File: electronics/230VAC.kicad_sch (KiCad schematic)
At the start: 11 parts, among them J21 Conn_01x02, J22 Conn_01x02, U13 CNY17-1, U17 H11AA1

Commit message: no tracks, but placement looks good
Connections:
- net GND is gone; now on net GND_LP: C9.2, U17.4
- net P_230VAC: now reaches J21.1 (Pin_1), R23.1
- net N_230VAC: now reaches J21.2 (Pin_2), R24.1
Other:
- moved on the sheet: J21
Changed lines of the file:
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@@
-	(wire
-		(pts
-			(xy 81.28 67.31) (xy 76.2 67.31)
-		)
-		(stroke
-			(width 0)
-			(type default)
-		)
-	)
 	(wire
 		(pts
@@
 	(wire
 		(pts
-			(xy 81.28 66.04) (xy 81.28 67.31)
+			(xy 81.28 68.58) (xy 81.28 66.04)
 		)
 		(stroke
@@
 	(wire
 		(pts
-			(xy 76.2 69.85) (xy 81.28 69.85)
-		)
-		(stroke
-			(width 0)
-			(type default)
-		)
-	)
-	(wire
-		(pts
-			(xy 81.28 69.85) (xy 81.28 71.12)
+			(xy 58.42 71.12) (xy 83.82 71.12)
 		)
 		(stroke
@@
 	(wire
 		(pts
-			(xy 81.28 71.12) (xy 83.82 71.12)
-		)
-		(stroke
-			(width 0)
-			(type default)
-		)
-	)
-	(wire
-		(pts
 			(xy 57.15 107.95) (xy 64.77 107.95)
 		)
@@
 	(wire
 		(pts
+			(xy 58.42 68.58) (xy 81.28 68.58)
+		)
+		(stroke
+			(width 0)
+			(type default)
+		)
+	)
+	(wire
+		(pts
 			(xy 120.65 120.65) (xy 147.32 120.65)
 		)
@@
 	)
 	(rectangle
-		(start 64.77 48.26)
+		(start 52.07 48.26)
 		(end 149.86 85.09)
 		(stroke
@@
 		)
 	)
-	(label "V_Bat"
-		(at 110.49 96.52 0)
+	(label "N_230VAC"
+		(at 67.31 71.12 0)
 		(fields_autoplaced yes)
 		(effects
@@
 		)
 	)
+	(label "P_230VAC"
+		(at 67.31 68.58 0)
+		(fields_autoplaced yes)
+		(effects
+			(font
+				(size 1.27 1.27)
+			)
+			(justify left bottom)
+		)
+	)
+	(label "V_Bat"
+		(at 110.49 96.52 0)
+		(fields_autoplaced yes)
+		(effects
+			(font
+				(size 1.27 1.27)
+			)
+			(justify left bottom)
+		)
+	)
 	(hierarchical_label "AC_DETECT"
 		(shape output)
@@
 		(lib_name "Conn_01x02_1")
 		(lib_id "Connector_Generic:Conn_01x02")
-		(at 71.12 69.85 180)
+		(at 53.34 71.12 180)
 		(unit 1)
 		(exclude_from_sim no)
@@
 		(fields_autoplaced yes)
 		(property "Reference" "J21"
-			(at 71.12 60.96 0)
+			(at 53.34 62.23 0)
 			(effects
 				(font
@@
 		)
 		(property "Value" "Conn_01x02"
-			(at 71.12 63.5 0)
+			(at 53.34 64.77 0)
 			(effects
 				(font
@@
 		)
 		(property "Footprint" "TerminalBlock:TerminalBlock_Xinya_XY308-2.54-2P_1x02_P2.54mm_Horizontal"
-			(at 71.12 69.85 0)
+			(at 53.34 71.12 0)
 			(effects
 				(font
@@
 		)
 		(property "Datasheet" "~"
-			(at 71.12 69.85 0)
+			(at 53.34 71.12 0)
 			(effects
 				(font
@@
 		)
 		(property "Description" "Generic connector, single row, 01x02, script generated (kicad-library-utils/schlib/autogen/connector/)"
-			(at 71.12 69.85 0)
+			(at 53.34 71.12 0)
 			(effects
 				(font
@@
 	)
 	(symbol
-		(lib_id "power:GND")
-		(at 116.84 74.93 0)
-		(unit 1)
-		(exclude_from_sim no)
-		(in_bom yes)
-		(on_board yes)
-		(dnp no)
-		(fields_autoplaced yes)
-		(property "Reference" "#PWR046"
-			(at 116.84 81.28 0)
-			(effects
-				(font
-					(size 1.27 1.27)
-				)
-				(hide yes)
-			)
-		)
-		(property "Value" "GND"
-			(at 116.84 80.01 0)
-			(effects
-				(font
-					(size 1.27 1.27)
-				)
-			)
-		)
-		(property "Footprint" ""
-			(at 116.84 74.93 0)
-			(effects
-				(font
-					(size 1.27 1.27)
-				)
-				(hide yes)
-			)
-		)
-		(property "Datasheet" ""
-			(at 116.84 74.93 0)
-			(effects
-				(font
-					(size 1.27 1.27)
-				)
-				(hide yes)
-			)
-		)
-		(property "Description" "Power symbol creates a global label with name \"GND\" , ground"
-			(at 116.84 74.93 0)
-			(effects
-				(font
-					(size 1.27 1.27)
-				)
-				(hide yes)
-			)
-		)
-		(pin "1"
-		)
-		(instances
-			(project "electronics"
-				(path "/eeb1234c-eae0-4ac6-a30d-2a978d66d889/04c402f1-b99a-4823-99a0-0c7312782f29/b07c78d9-bf9b-4530-b7c9-2098e4c7b5ee"
-					(reference "#PWR046")
-					(unit 1)
-				)
-			)
-		)
-	)
-	(symbol
 		(lib_id "Connector_Generic:Conn_01x02")
 		(at 160.02 107.95 0)
@@
 					(unit 1)
 				)
+			)
+		)
+	)
+	(symbol
+		(lib_id "power:GND2")
+		(at 116.84 74.93 0)
+		(unit 1)
+		(exclude_from_sim no)
+		(in_bom yes)
+		(on_board yes)
+		(dnp no)
+		(fields_autoplaced yes)
+		(property "Reference" "#PWR037"
+			(at 116.84 81.28 0)
+			(effects
+				(font
+					(size 1.27 1.27)
+				)
+				(hide yes)
+			)
+		)
+		(property "Value" "GND_LP"
+			(at 116.84 80.01 0)
+			(effects
+				(font
+					(size 1.27 1.27)
+				)
+			)
+		)
+		(property "Footprint" ""
+			(at 116.84 74.93 0)
+			(effects
+				(font
+					(size 1.27 1.27)
+				)
+				(hide yes)
+			)
+		)
+		(property "Datasheet" ""
+			(at 116.84 74.93 0)
+			(effects
+				(font
+					(size 1.27 1.27)
+				)
+				(hide yes)
+			)
+		)
+		(property "Description" "Power symbol creates a global label with name \"GND2\" , ground"
+			(at 116.84 74.93 0)
+			(effects
+				(font
+					(size 1.27 1.27)
+				)
+				(hide yes)
+			)
+		)
+		(pin "1"
+		)
+		(instances
+			(project "electronics"
+				(path "/eeb1234c-eae0-4ac6-a30d-2a978d66d889/04c402f1-b99a-4823-99a0-0c7312782f29/b07c78d9-bf9b-4530-b7c9-2098e4c7b5ee"
+					(reference "#PWR037")
+					(unit 1)
+				)

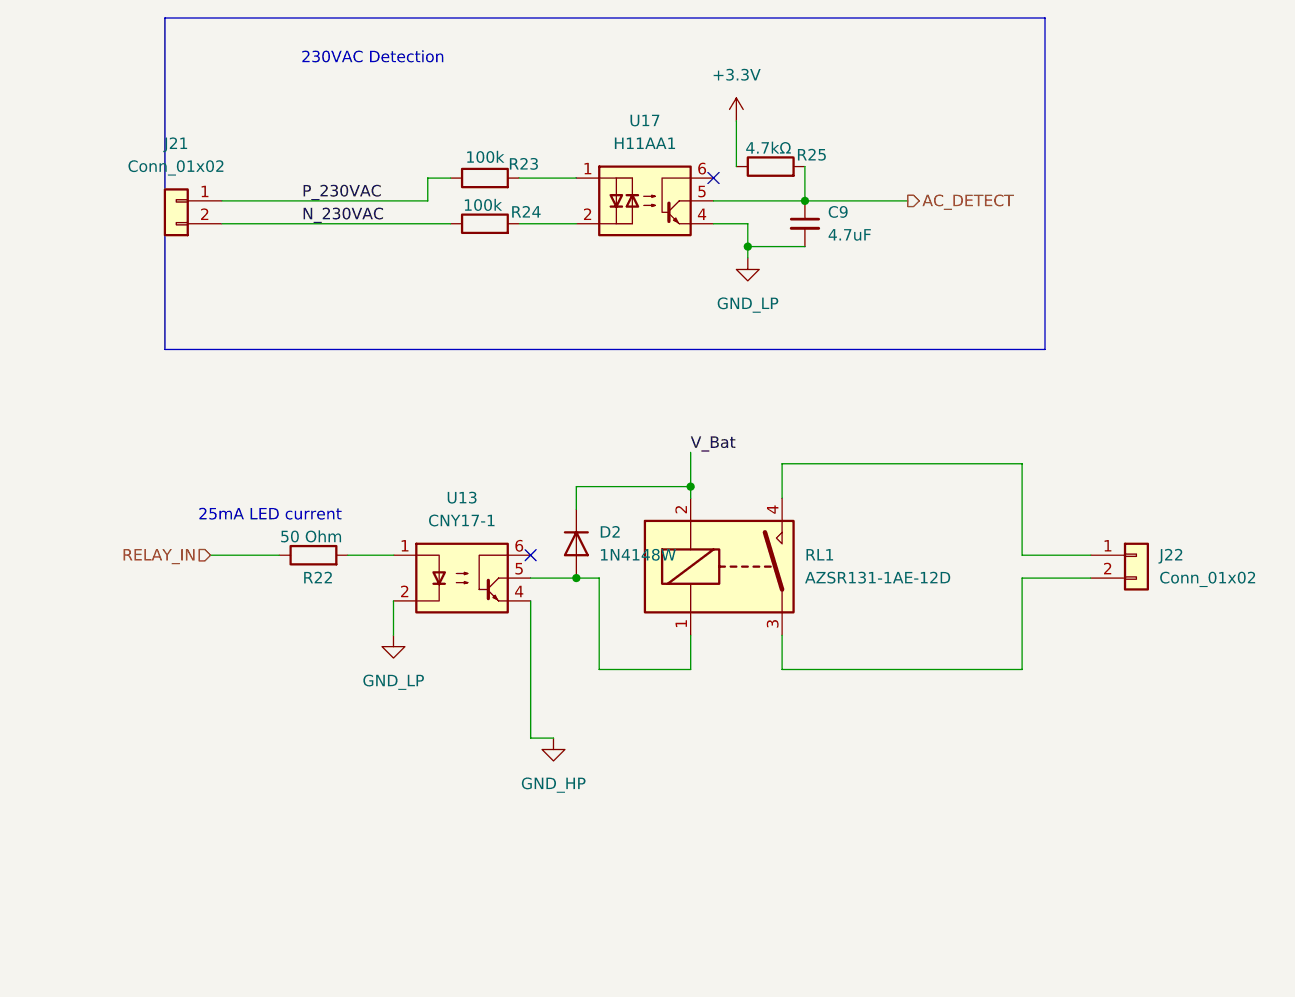
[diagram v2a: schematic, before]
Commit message: start to create BOM and finalising symbol fields
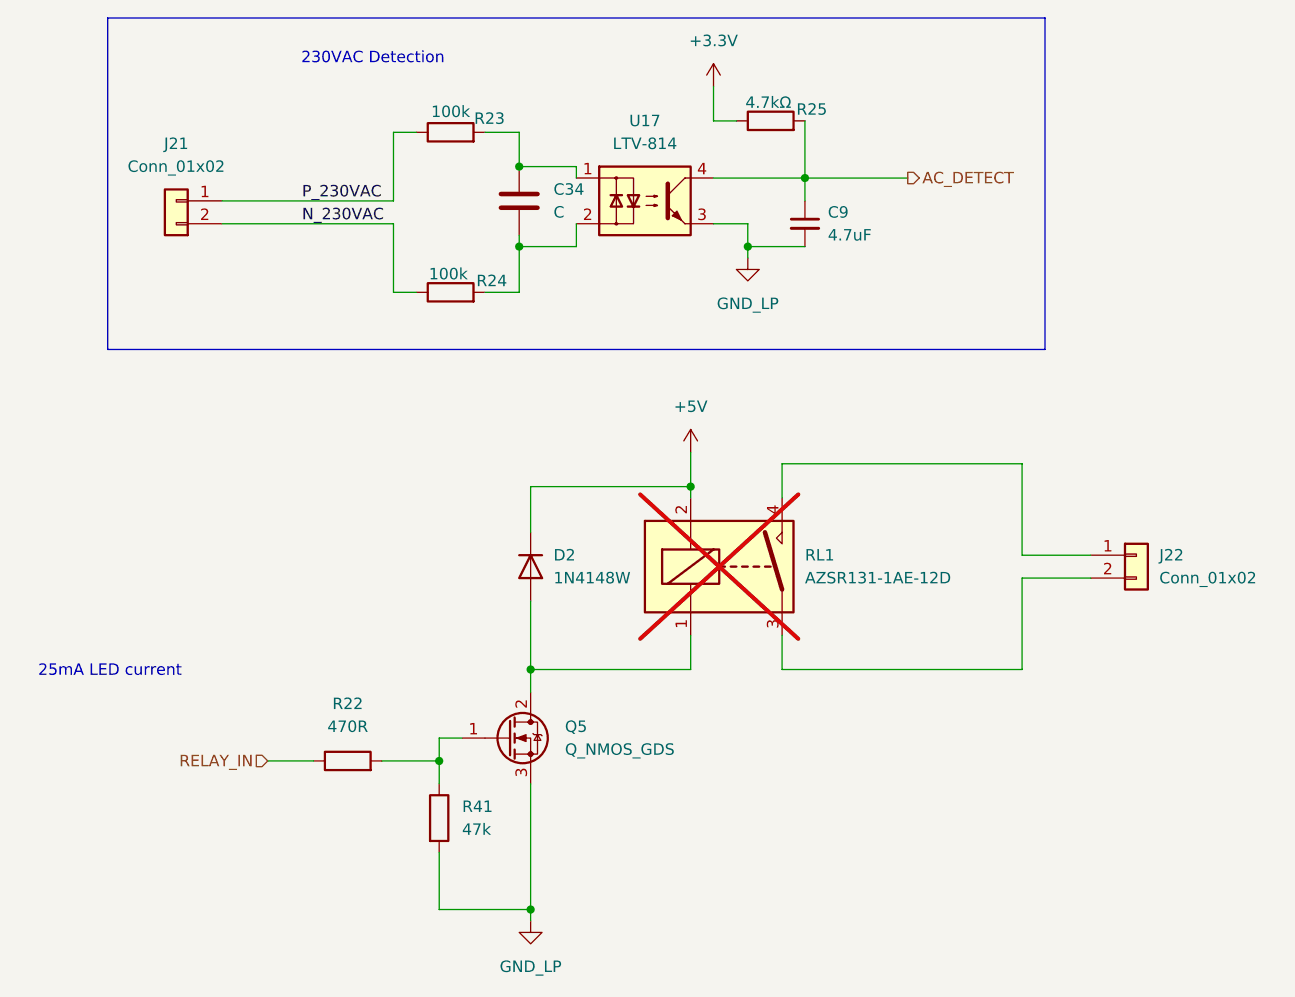
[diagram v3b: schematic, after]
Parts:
- removed U13: CNY17-1, Package_TO_SOT_SMD:SOT-23-6, symbol Isolator:CNY17-1
- removed U17: H11AA1, Package_DIP:DIP-6_W7.62mm, symbol Isolator:H11AA1
- added C34: C, Capacitor_THT:C_Disc_D3.0mm_W2.0mm_P2.50mm, symbol Device:C
- added Q5: Q_NMOS_GDS, Package_TO_SOT_SMD:TO-252-2, symbol Device:Q_NMOS_GDS
- added R41: 47k, Resistor_SMD:R_0805_2012Metric, symbol Device:R
- added U17: LTV-814, Package_DIP:DIP-4_W7.62mm, symbol Isolator:LTV-814
- C9: footprint Capacitor_SMD:C_0805_2012Metric_Pad1.18x1.45mm_HandSolder -> Capacitor_SMD:C_0805_2012Metric
- D2: MFG part nr (none) -> 1N4148W; Manufacturer (none) -> Vishay; lcsc (none) -> C917030; mouser (none) -> 821-1N4148W-GRHG
- R22: value 50 Ohm -> 470R; footprint Resistor_SMD:R_0805_2012Metric_Pad1.20x1.40mm_HandSolder -> Resistor_SMD:R_0805_2012Metric
- R25: footprint Resistor_SMD:R_0805_2012Metric_Pad1.20x1.40mm_HandSolder -> Resistor_SMD:R_0805_2012Metric
- RL1: MFG Part Nr (none) -> PRE29-5V-S-450; Manufacturer (none) -> same sky; now not fitted
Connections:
- net AC_DETECT: now also U17.4
- net GND_LP: now also Q5.3 (S), R41.2, U17.3
- net at R23.2: now also C34.1, U17.1
- net at D2.2 (A), RL1.1: now also Q5.2 (D)
- net at R22.2: now also Q5.1 (G), R41.1
- net at R24.2: now also C34.2, U17.2
- net V_Bat renamed +5V
- no-connect marks 2 -> 0
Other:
- moved on the sheet: D2, R23, R24, R25

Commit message: progres on layouting
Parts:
- Q5: footprint Package_TO_SOT_SMD:TO-252-2 -> Package_TO_SOT_SMD:SOT-23
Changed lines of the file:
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@@
 	(label "N_230VAC"
 		(at 67.31 71.12 0)
-		(fields_autoplaced yes)
 		(effects
 			(font
@@
 	(label "P_230VAC"
 		(at 67.31 68.58 0)
-		(fields_autoplaced yes)
 		(effects
 			(font
@@
 		(shape output)
 		(at 134.62 66.04 0)
-		(fields_autoplaced yes)
 		(effects
 			(font
@@
 		(shape input)
 		(at 63.5 130.81 180)
-		(fields_autoplaced yes)
 		(effects
 			(font
@@
 			)
 		)
-		(property "Footprint" "Package_TO_SOT_SMD:TO-252-2"
+		(property "Footprint" "Package_TO_SOT_SMD:SOT-23"
 			(at 95.25 125.73 0)
 			(effects
